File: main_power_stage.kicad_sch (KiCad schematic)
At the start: 69 parts, among them SW1 CAS-120TA, U2 LV14540DDAR, U6 TPS65987DDHRSHR, U7 LV14540DDAR, U8 74CBTLV3257_VQFN, U9 W25Q80DV_SOIC-8

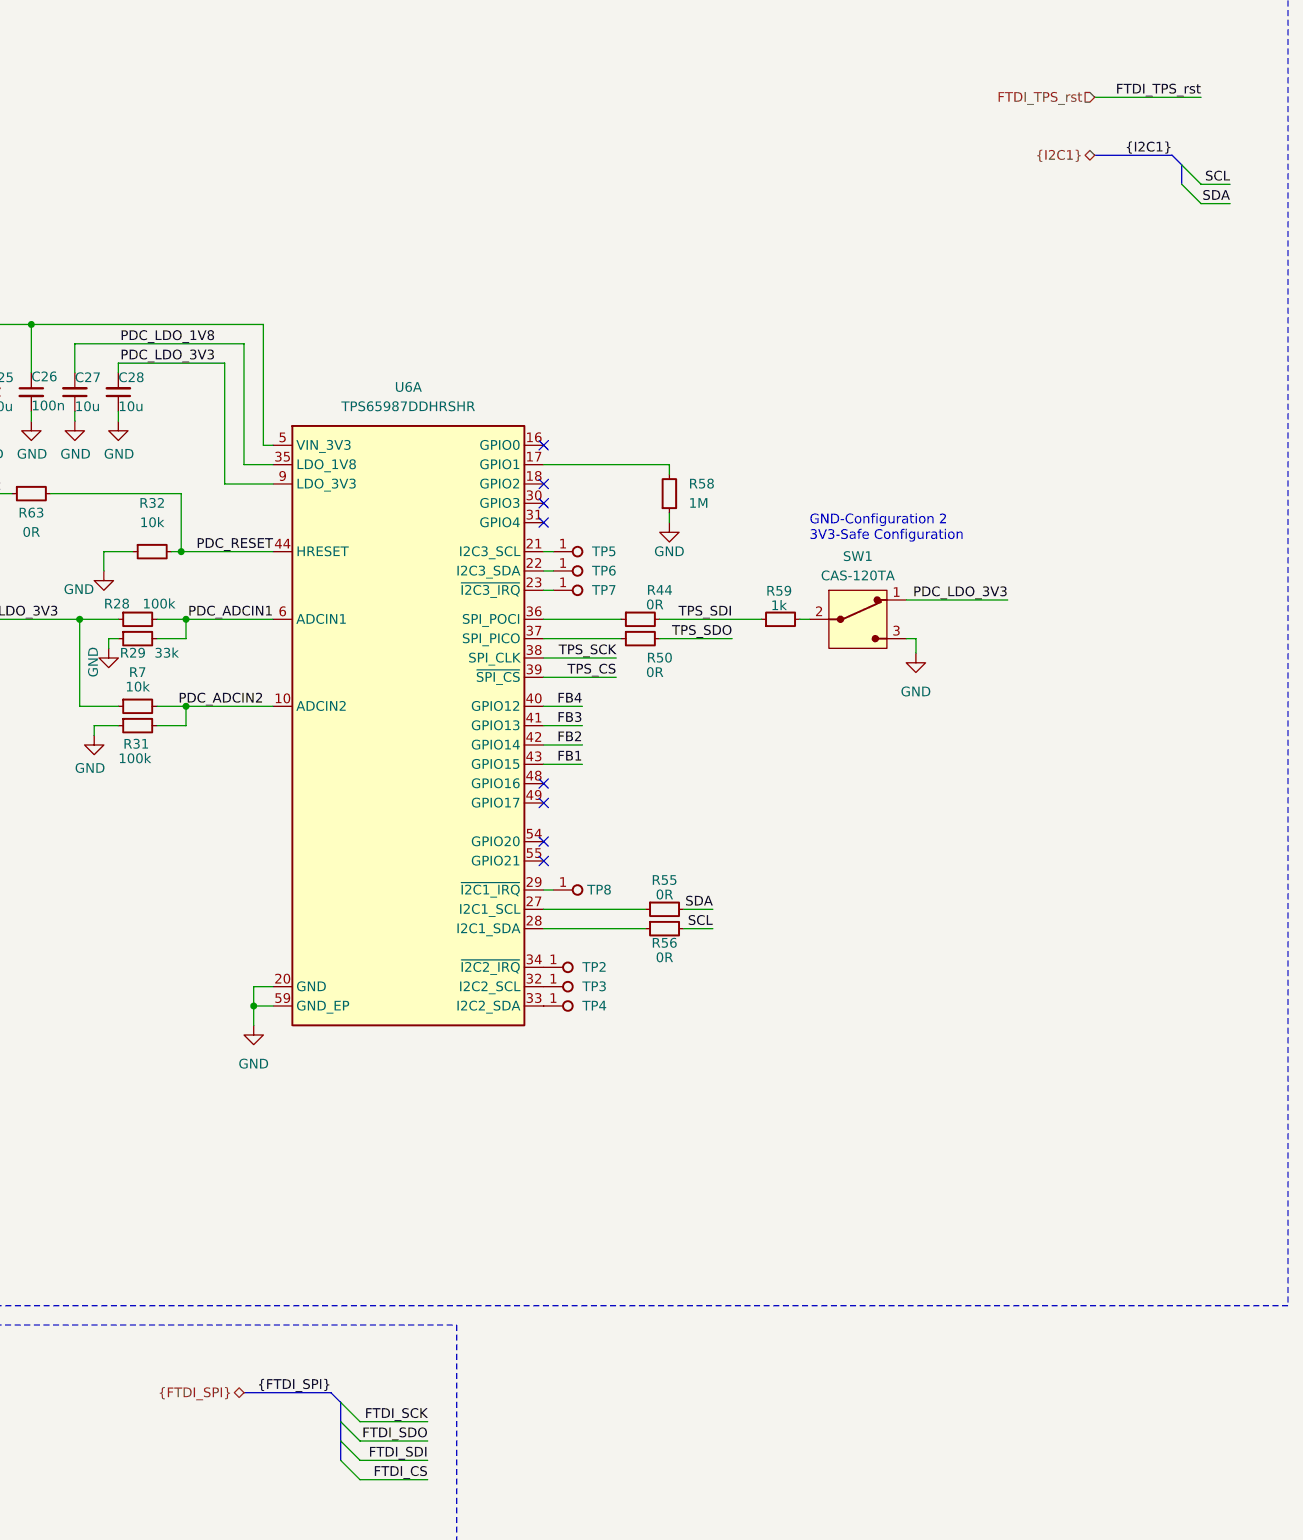
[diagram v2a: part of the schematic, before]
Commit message: [#62835] PoE to USB-C PD Review Rev.1.0.0 correct points 1,3,4,6,7,11
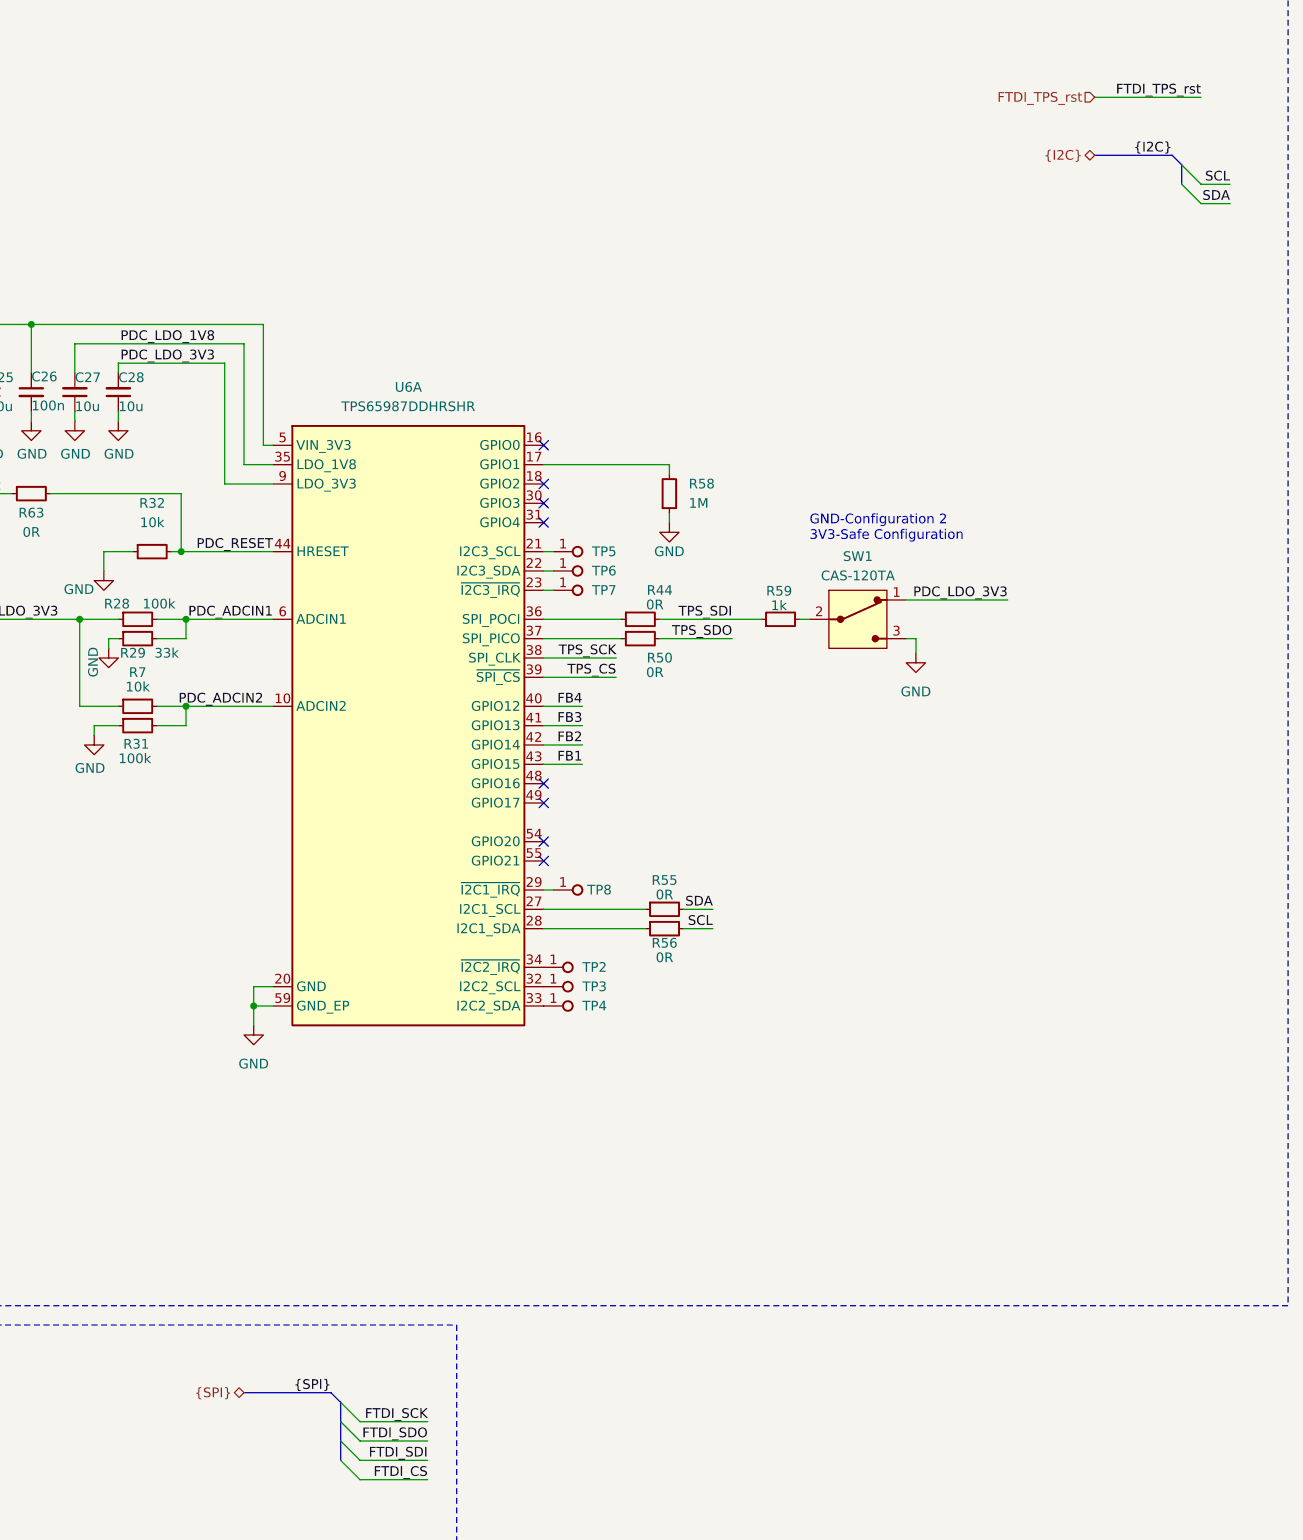
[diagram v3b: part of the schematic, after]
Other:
- company: (none) -> Antmicro ltd.
- title: (none) -> PoE to USBC PD adapter
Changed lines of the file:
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@@
 (kicad_sch (version 20230121) (generator eeschema)
   (paper "A3")
-  (bus_alias "I2C1" (members "SCL" "SDA"))
+  (title_block
+    (title "PoE to USBC PD adapter")
+    (date "2024-07-08")
+    (company "Antmicro ltd.")
+  )
+  (bus_alias "I2C" (members "SCL" "SDA"))
   (junction (at 235.585 57.785) (diameter 0) (color 0 0 0 0)
   )
@@
     (effects (font (size 1.27 1.27)) (justify right bottom))
   )
-  (label "{FTDI_SPI}" (at 280.67 198.12 180) (fields_autoplaced)
+  (label "{SPI}" (at 280.67 198.12 180) (fields_autoplaced)
     (effects (font (size 1.27 1.27)) (justify right bottom))
   )
@@
     (effects (font (size 1.27 1.27)) (justify right bottom))
   )
-  (label "{I2C1}" (at 391.16 35.56 180) (fields_autoplaced)
+  (label "{I2C}" (at 391.16 35.56 180) (fields_autoplaced)
     (effects (font (size 1.27 1.27)) (justify right bottom))
   )
@@
     (effects (font (size 1.27 1.27)) (justify right))
   )
-  (hierarchical_label "{I2C1}" (shape bidirectional) (at 381 35.56 180) (fields_autoplaced)
+  (hierarchical_label "{I2C}" (shape bidirectional) (at 381 35.56 180) (fields_autoplaced)
     (effects (font (size 1.27 1.27)) (justify right))
   )
-  (hierarchical_label "{FTDI_SPI}" (shape bidirectional) (at 269.24 198.12 180) (fields_autoplaced)
+  (hierarchical_label "{SPI}" (shape bidirectional) (at 269.24 198.12 180) (fields_autoplaced)
     (effects (font (size 1.27 1.27)) (justify right))
   )

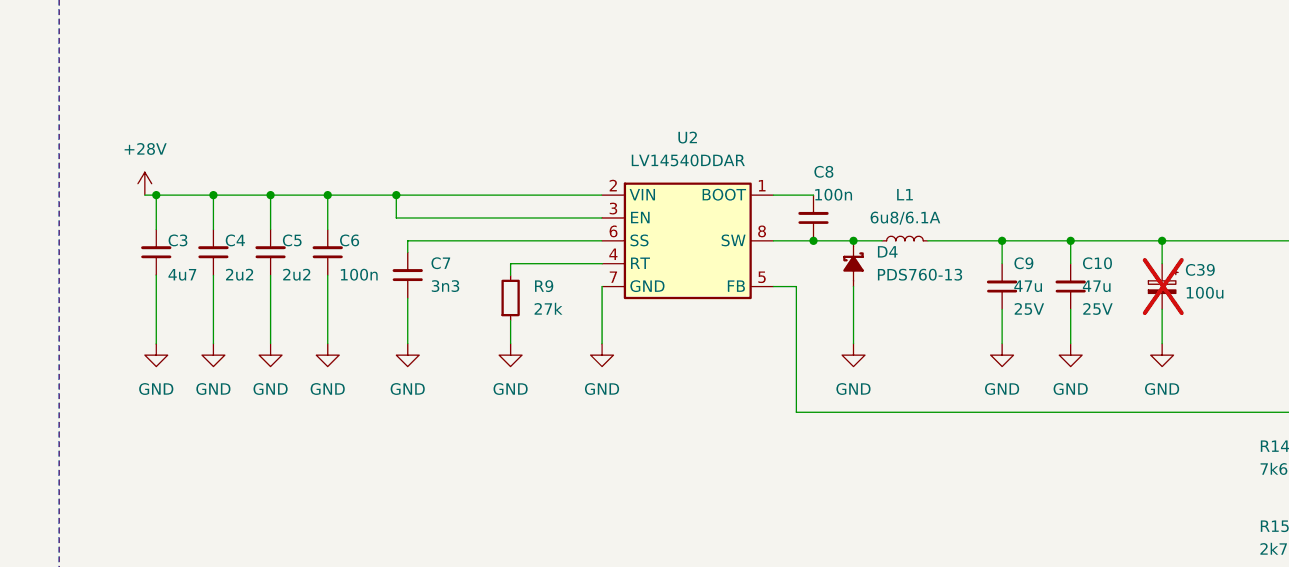
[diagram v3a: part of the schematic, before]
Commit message: [#62835] Add ETH receptacle diode steering
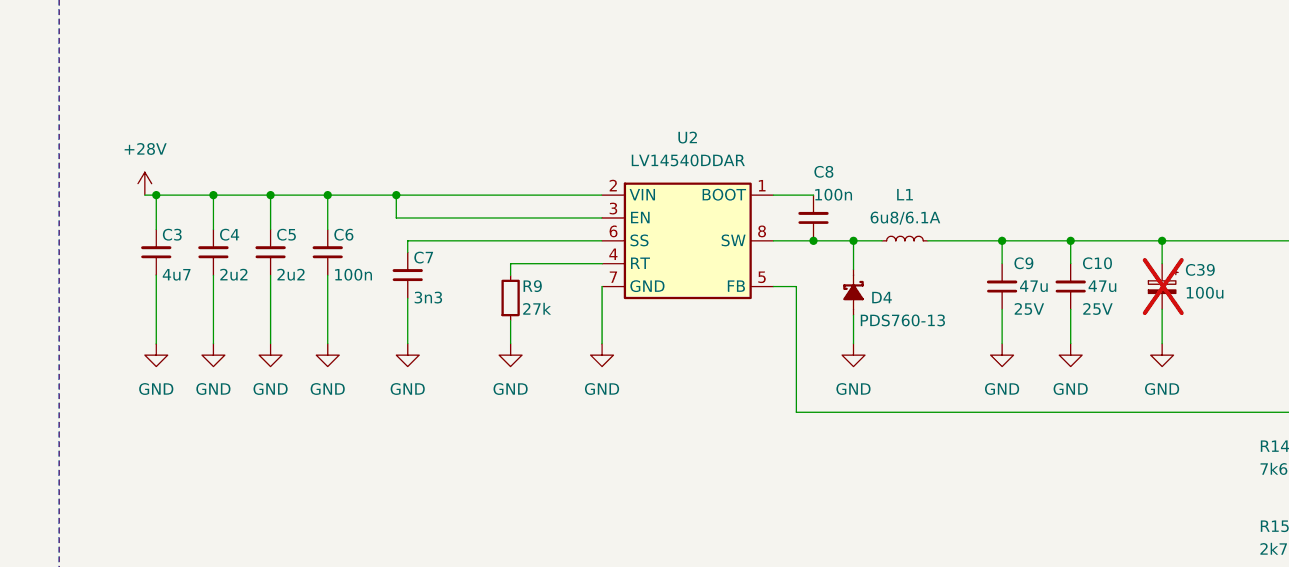
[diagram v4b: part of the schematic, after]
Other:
- moved on the sheet: D4
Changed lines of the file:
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@@
     (stroke (width 0) (type default))
   )
-  (wire (pts (xy 102.235 48.26) (xy 102.235 54.61))
+  (wire (pts (xy 102.235 51.435) (xy 102.235 54.61))
     (stroke (width 0) (type default))
   )
@@
     (stroke (width 0) (type default))
   )
+  (wire (pts (xy 102.235 46.355) (xy 102.235 43.18))
+    (stroke (width 0) (type default))
+  )
   (wire (pts (xy 153.67 222.25) (xy 163.195 222.25))
     (stroke (width 0) (type default))
@@
   )
   (symbol (lib_id "antmicroCapacitors0603:C_100n_100V_X7R_0603") (at 43.815 46.99 90) (unit 1)
-    (in_bom yes) (on_board yes) (dnp no)
-    (property "Reference" "C6" (at 45.085 43.18 90)
+    (in_bom yes) (on_board yes) (dnp no) (fields_autoplaced)
+    (property "Reference" "C6" (at 44.45 42.545 90)
       (effects (font (size 1.27 1.27) (thickness 0.15)) (justify right))
     )
@@
       (effects (font (size 1.27 1.27) (thickness 0.15)) (justify left bottom) hide)
     )
-    (property "Val" "100n" (at 45.085 46.99 90)
+    (property "Val" "100n" (at 44.45 46.99 90)
       (effects (font (size 1.27 1.27) (thickness 0.15)) (justify right))
     )
@@
     )
   )
-  (symbol (lib_id "antmicroDiodesRectifiersSingle:PDS760") (at 102.235 43.18 270) (unit 1)
-    (in_bom yes) (on_board yes) (dnp no) (fields_autoplaced)
-    (property "Reference" "D4" (at 104.775 44.45 90)
+  (symbol (lib_id "antmicroDiodesRectifiersSingle:PDS760") (at 102.235 46.355 270) (unit 1)
+    (in_bom yes) (on_board yes) (dnp no)
+    (property "Reference" "D4" (at 104.14 49.53 90)
       (effects (font (size 1.27 1.27) (thickness 0.15)) (justify left))
     )
-    (property "Value" "PDS760" (at 84.455 66.04 0)
+    (property "Value" "PDS760" (at 84.455 69.215 0)
       (effects (font (size 1.27 1.27) (thickness 0.15)) (justify left bottom) hide)
     )
-    (property "Footprint" "antmicro-footprints:PowerDI5" (at 92.075 66.04 0)
+    (property "Footprint" "antmicro-footprints:PowerDI5" (at 92.075 69.215 0)
       (effects (font (size 1.27 1.27) (thickness 0.15)) (justify left bottom) hide)
     )
-    (property "Datasheet" "https://www.diodes.com/assets/Datasheets/ds30470.pdf" (at 89.535 66.04 0)
+    (property "Datasheet" "https://www.diodes.com/assets/Datasheets/ds30470.pdf" (at 89.535 69.215 0)
       (effects (font (size 1.27 1.27) (thickness 0.15)) (justify left bottom) hide)
     )
-    (property "Manufacturer" "Diodes Incorporated" (at 86.995 66.04 0)
+    (property "Manufacturer" "Diodes Incorporated" (at 86.995 69.215 0)
       (effects (font (size 1.27 1.27) (thickness 0.15)) (justify left bottom) hide)
     )
-    (property "MPN" "PDS760-13" (at 104.775 46.99 90)
+    (property "MPN" "PDS760-13" (at 102.87 52.07 90)
       (effects (font (size 1.27 1.27) (thickness 0.15)) (justify left))
     )
-    (property "Author" "Antmicro" (at 81.915 66.04 0)
+    (property "Author" "Antmicro" (at 81.915 69.215 0)
       (effects (font (size 1.27 1.27) (thickness 0.15)) (justify left bottom) hide)
     )
-    (property "License" "Apache-2.0" (at 79.375 66.04 0)
+    (property "License" "Apache-2.0" (at 79.375 69.215 0)
       (effects (font (size 1.27 1.27) (thickness 0.15)) (justify left bottom) hide)
     )
@@
       (effects (font (size 1.27 1.27) (thickness 0.15)) (justify left bottom) hide)
     )
-    (property "Val" "47u" (at 120.015 48.26 90)
+    (property "Val" "47u" (at 120.65 48.26 90)
       (effects (font (size 1.27 1.27) (thickness 0.15)) (justify right))
     )
@@
   (symbol (lib_id "antmicroCapacitorsmisc:C_2u2_1210") (at 31.115 46.99 90) (unit 1)
     (in_bom yes) (on_board yes) (dnp no)
-    (property "Reference" "C4" (at 32.385 43.18 90)
+    (property "Reference" "C4" (at 31.75 42.545 90)
       (effects (font (size 1.27 1.27) (thickness 0.15)) (justify right))
     )
@@
       (effects (font (size 1.27 1.27) (thickness 0.15)) (justify left bottom) hide)
     )
-    (property "Val" "2u2" (at 32.385 46.99 90)
+    (property "Val" "2u2" (at 31.75 46.99 90)
       (effects (font (size 1.27 1.27) (thickness 0.15)) (justify right))
     )
@@
   (symbol (lib_id "antmicroCapacitors0402:C_3n3_0402") (at 52.705 49.53 90) (unit 1)
     (in_bom yes) (on_board yes) (dnp no) (fields_autoplaced)
-    (property "Reference" "C7" (at 55.245 45.7136 90)
+    (property "Reference" "C7" (at 53.34 45.085 90)
       (effects (font (size 1.27 1.27) (thickness 0.15)) (justify right))
     )
@@
       (effects (font (size 1.27 1.27) (thickness 0.15)) (justify left bottom) hide)
     )
-    (property "Val" "3n3" (at 55.245 48.2536 90)
+    (property "Val" "3n3" (at 53.34 49.53 90)
       (effects (font (size 1.27 1.27) (thickness 0.15)) (justify right))
     )
@@
   )
   (symbol (lib_id "antmicroResistors0402:R_27k_0402") (at 64.135 52.07 90) (unit 1)
-    (in_bom yes) (on_board yes) (dnp no) (fields_autoplaced)
-    (property "Reference" "R9" (at 66.675 48.26 90)
+    (in_bom yes) (on_board yes) (dnp no)
+    (property "Reference" "R9" (at 65.405 48.26 90)
       (effects (font (size 1.27 1.27) (thickness 0.15)) (justify right))
     )
@@
       (effects (font (size 1.27 1.27) (thickness 0.15)) (justify left bottom) hide)
     )
-    (property "Val" "27k" (at 66.675 50.8 90)
+    (property "Val" "27k" (at 65.405 50.8 90)
       (effects (font (size 1.27 1.27) (thickness 0.15)) (justify right))
     )
@@
   )
   (symbol (lib_id "antmicroCapacitorsmisc:C_2u2_1210") (at 37.465 46.99 90) (unit 1)
-    (in_bom yes) (on_board yes) (dnp no)
-    (property "Reference" "C5" (at 38.735 43.18 90)
+    (in_bom yes) (on_board yes) (dnp no) (fields_autoplaced)
+    (property "Reference" "C5" (at 38.1 42.545 90)
       (effects (font (size 1.27 1.27) (thickness 0.15)) (justify right))
     )
@@
       (effects (font (size 1.27 1.27) (thickness 0.15)) (justify left bottom) hide)
     )
-    (property "Val" "2u2" (at 38.735 46.99 90)
+    (property "Val" "2u2" (at 38.1 46.99 90)
       (effects (font (size 1.27 1.27) (thickness 0.15)) (justify right))
     )
@@
       (effects (font (size 1.27 1.27) (thickness 0.15)) (justify left bottom) hide)
     )
-    (property "Val" "47u" (at 127.635 48.26 90)
+    (property "Val" "47u" (at 128.27 48.26 90)
       (effects (font (size 1.27 1.27) (thickness 0.15)) (justify right))
     )
@@
   (symbol (lib_id "antmicroCapacitorsmisc:C_4u7_1210_100V") (at 24.765 46.99 90) (unit 1)
     (in_bom yes) (on_board yes) (dnp no)
-    (property "Reference" "C3" (at 26.035 43.18 90)
+    (property "Reference" "C3" (at 25.4 42.545 90)
       (effects (font (size 1.27 1.27) (thickness 0.15)) (justify right))
     )
@@
       (effects (font (size 1.27 1.27) (thickness 0.15)) (justify left bottom) hide)
     )
-    (property "Val" "4u7" (at 26.035 46.99 90)
+    (property "Val" "4u7" (at 25.4 46.99 90)
       (effects (font (size 1.27 1.27) (thickness 0.15)) (justify right))
     )

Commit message: [#62835] Change L3 3V3 buck and divider, to 5V dcdc buck
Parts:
- removed L2: L_33u_0.42A_WE-TPC-3816, antmicro-footprints:L_WE-TPC-3816, symbol antmicroFixedInductors:L_33u_0.42A_WE-TPC-3816
- removed R26: R_59k_0402, antmicro-footprints:R_0402_1005Metric, symbol antmicroResistors0402:R_59k_0402
- added L3: L_4u7_1.55A_Bourns-SRP2512A, antmicro-footprints:L_Bourns-SRP2512A, symbol antmicroFixedInductors:L_4u7_1.55A_Bourns-SRP2512A
- added R26: R_33k_0402, antmicro-footprints:R_0402_1005Metric, symbol antmicroResistors0402:R_33k_0402
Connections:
- net +3V3: no longer C23.2, C24.2, R25.2
- net GND: now also R26.1
- net at R25.1, U7.5 (FB): now also R26.2
- net at C22.1, D5.1 (C), U7.8 (SW): now also L3.1
- new net +5V: C23.2, C24.2, L3.2, R25.2
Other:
- note added: "3V3 LDO"
- note added: "5V buck"
- note removed: "3V3 buck"
- moved on the sheet: C40, R42, R43, R57, R62, U8
